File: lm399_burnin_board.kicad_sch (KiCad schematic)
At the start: 12 parts, among them J1 C64AC, J2 DB50_Female, U26 LT1085-ADJ

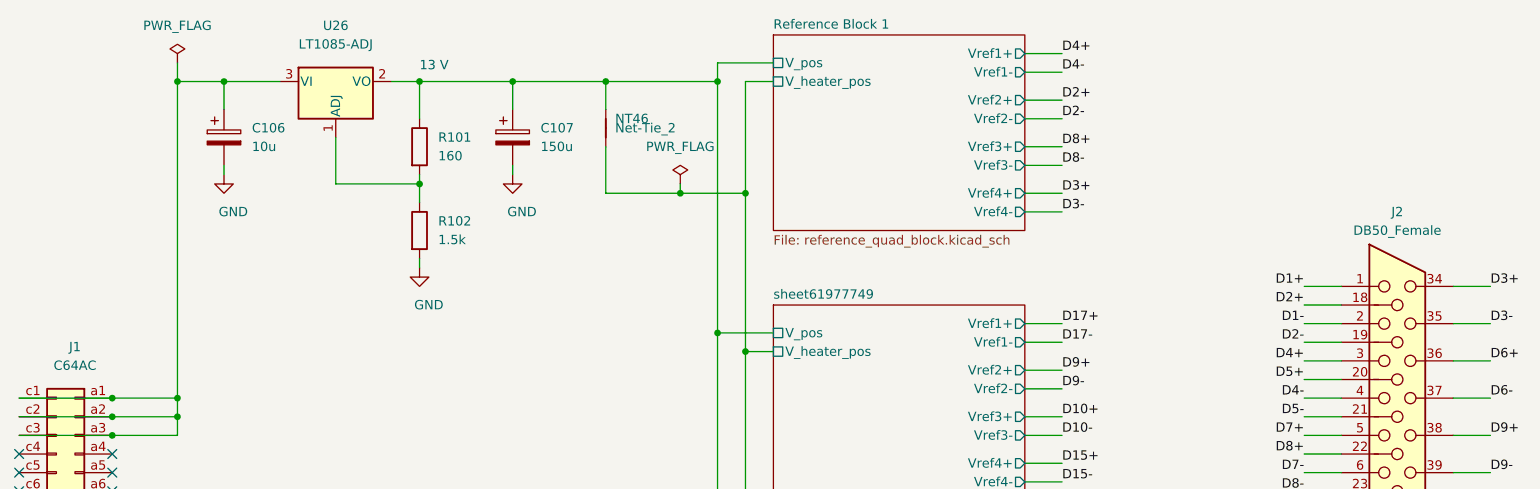
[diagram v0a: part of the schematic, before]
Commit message: Updated references to follow geographical rules
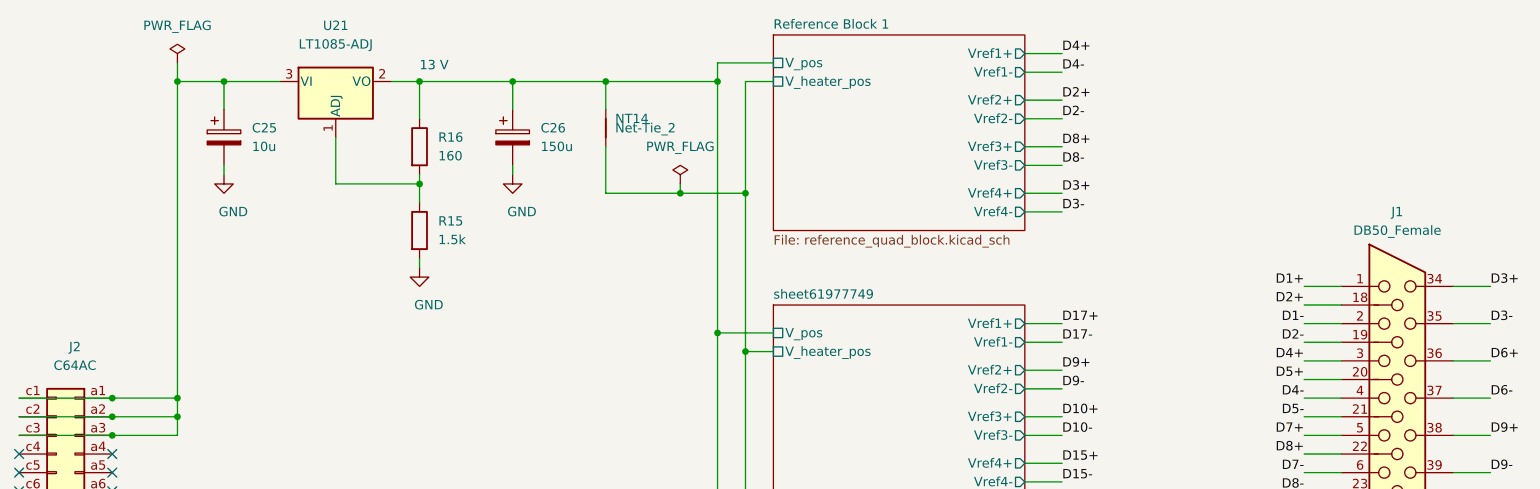
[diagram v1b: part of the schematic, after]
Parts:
- renumbered C106 to C25, C107 to C26, J2 to J1, J1 to J2, NT46 to NT14, R102 to R15, R101 to R16, U26 to U21
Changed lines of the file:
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@@
 		(on_board yes)
 		(dnp no)
-		(property "Reference" "J1"
+		(property "Reference" "J2"
 			(at 26.67 60.325 0)
 			(effects
@@
 			(project "lm399_burnin_board"
 				(path "/6284122b-79c3-4e04-925e-3d32cc3ec077"
-					(reference "J1")
+					(reference "J2")
 					(unit 1)
 				)
@@
 		(on_board yes)
 		(dnp no)
-		(property "Reference" "J2"
+		(property "Reference" "J1"
 			(at 207.01 41.91 0)
 			(effects
@@
 			(project "main"
 				(path "/6284122b-79c3-4e04-925e-3d32cc3ec077"
-					(reference "J2")
+					(reference "J1")
 					(unit 1)
 				)
@@
 		(on_board yes)
 		(dnp no)
-		(property "Reference" "U26"
+		(property "Reference" "U21"
 			(at 62.23 16.51 0)
 			(effects
@@
 			(project "main"
 				(path "/6284122b-79c3-4e04-925e-3d32cc3ec077"
-					(reference "U26")
+					(reference "U21")
 					(unit 1)
 				)
@@
 		(on_board yes)
 		(dnp no)
-		(property "Reference" "C106"
+		(property "Reference" "C25"
 			(at 50.8 30.48 0)
 			(effects
@@
 			(project "main"
 				(path "/6284122b-79c3-4e04-925e-3d32cc3ec077"
-					(reference "C106")
+					(reference "C25")
 					(unit 1)
 				)
@@
 		(on_board yes)
 		(dnp no)
-		(property "Reference" "C107"
+		(property "Reference" "C26"
 			(at 90.17 30.48 0)
 			(effects
@@
 			(project "main"
 				(path "/6284122b-79c3-4e04-925e-3d32cc3ec077"
-					(reference "C107")
+					(reference "C26")
 					(unit 1)
 				)
@@
 		(on_board yes)
 		(dnp no)
-		(property "Reference" "R101"
+		(property "Reference" "R16"
 			(at 76.2 31.75 0)
 			(effects
@@
 			(project "main"
 				(path "/6284122b-79c3-4e04-925e-3d32cc3ec077"
-					(reference "R101")
+					(reference "R16")
 					(unit 1)
 				)
@@
 		(on_board yes)
 		(dnp no)
-		(property "Reference" "R102"
+		(property "Reference" "R15"
 			(at 76.2 43.18 0)
 			(effects
@@
 			(project "main"
 				(path "/6284122b-79c3-4e04-925e-3d32cc3ec077"
-					(reference "R102")
+					(reference "R15")
 					(unit 1)
 				)
@@
 		(on_board yes)
 		(dnp no)
-		(property "Reference" "NT46"
+		(property "Reference" "NT14"
 			(at 100.33 29.21 90)
 			(effects
@@
 			(project "main"
 				(path "/6284122b-79c3-4e04-925e-3d32cc3ec077"
-					(reference "NT46")
+					(reference "NT14")
 					(unit 1)
 				)

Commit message: Fixed footprints
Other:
- sheet sheet61977749 renamed Reference Block 2
- sheet sheet61977B89 renamed Reference Block 3
- sheet sheet6197811F renamed Reference Block 4
- sheet sheet6197BEAD renamed Reference Block 5
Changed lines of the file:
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@@
 			)
 		)
-		(property "Datasheet" " ~"
+		(property "Datasheet" "~"
 			(at 182.88 80.01 0)
 			(effects
@@
 		(at 256.54 171.45 0)
 		(unit 1)
-		(exclude_from_sim no)
+		(exclude_from_sim yes)
 		(in_bom yes)
 		(on_board yes)
@@
 		)
 		(property "PN" ""
-			(at 256.54 171.45 0)
-			(effects
-				(font
-					(size 1.27 1.27)
-				)
-				(hide yes)
-			)
-		)
-		(property "Sim.Enable" "0"
 			(at 256.54 171.45 0)
 			(effects
@@
 			(color 0 0 0 0.0000)
 		)
-		(property "Sheetname" "sheet61977749"
+		(property "Sheetname" "Reference Block 2"
 			(at 121.92 53.8984 0)
 			(effects
@@
 			(color 0 0 0 0.0000)
 		)
-		(property "Sheetname" "sheet61977B89"
+		(property "Sheetname" "Reference Block 3"
 			(at 121.92 90.7284 0)
 			(effects
@@
 			(color 0 0 0 0.0000)
 		)
-		(property "Sheetname" "sheet6197811F"
+		(property "Sheetname" "Reference Block 4"
 			(at 121.92 127.5584 0)
 			(effects
@@
 			(color 0 0 0 0.0000)
 		)
-		(property "Sheetname" "sheet6197BEAD"
+		(property "Sheetname" "Reference Block 5"
 			(at 121.92 164.3884 0)
 			(effects

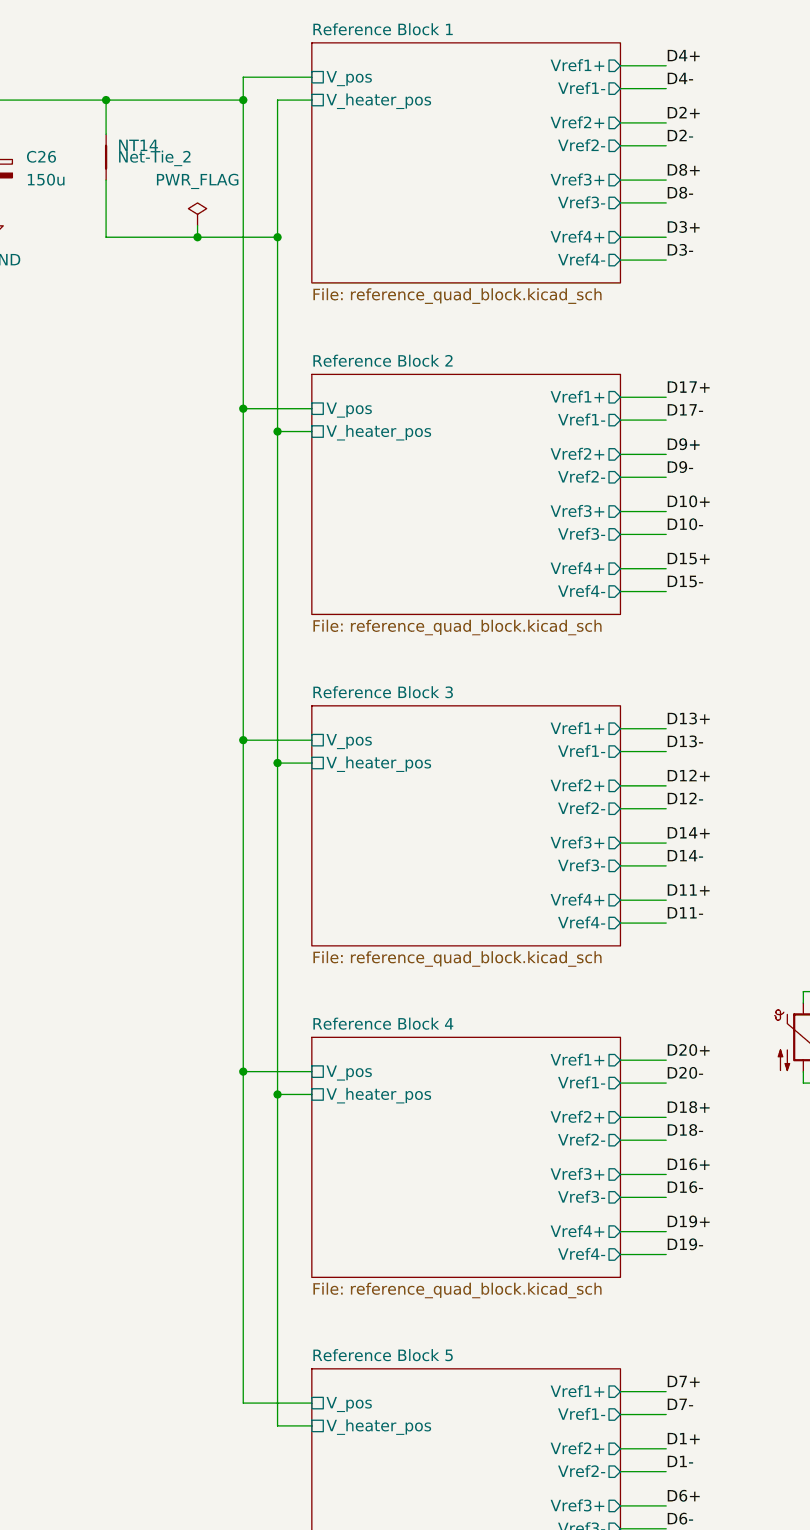
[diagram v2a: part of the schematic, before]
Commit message: Added CI (#6)
* Added CI

* Added RoHS info

* Fixed silkscreen labels
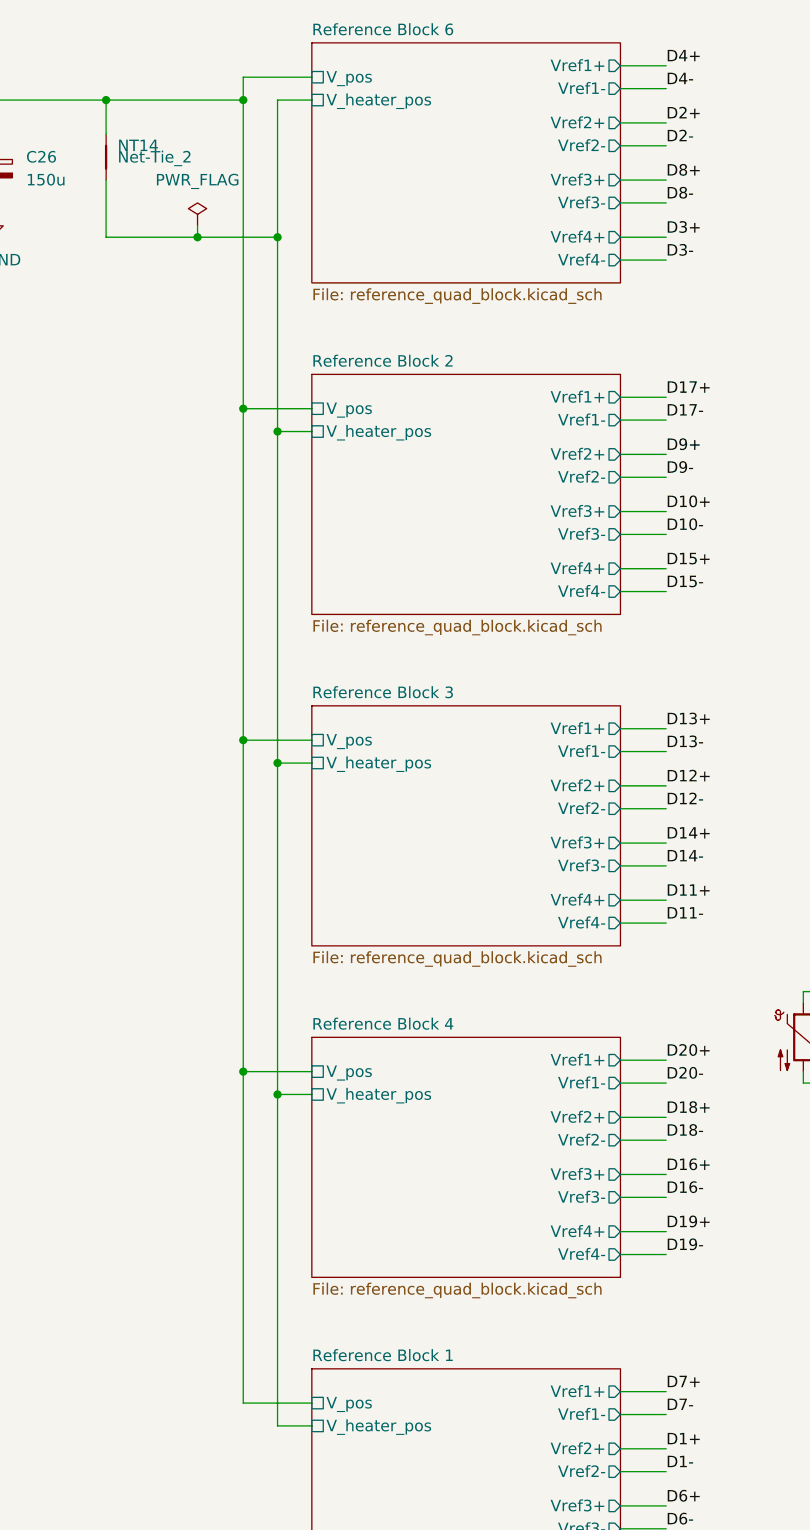
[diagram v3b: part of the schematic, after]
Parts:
- C25, C26: RoHS (none) -> Yes; Temperature (none) -> Tstorage = –55 °C to 105 °C
- J1: RoHS (none) -> Yes; Temperature (none) -> Tstorage = –55 °C to 125 °C
- J2: MFN Erni -> HARTING; PN 364914 -> 09031646921; RoHS (none) -> Yes; Temperature (none) -> Tstorage = –55 °C to 125 °C
- R15, R16: RoHS (none) -> By exemption; Temperature (none) -> Tstorage = –55 °C to 155 °C
- TH1, TH2: RoHS (none) -> Yes; Temperature (none) -> Tstorage = –40 °C to 150 °C
- U21: RoHS (none) -> By exemption; Temperature (none) -> Tstorage = –40 °C to 150 °C
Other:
- removed sheet Reference Block 5
- added sheet Reference Block 6 (reference_quad_block.kicad_sch)
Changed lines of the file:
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@@
 			)
 		)
-		(property "Description" ""
+		(property "Description" "DIN41612 connector, double row (AC), 02x32, script generated (kicad-library-utils/schlib/autogen/connector/)"
 			(at 26.67 105.41 0)
 			(effects
@@
 			)
 		)
-		(property "MFN" "Erni"
+		(property "MFN" "HARTING"
 			(at 26.67 105.41 0)
 			(effects
@@
 			)
 		)
-		(property "PN" "364914"
+		(property "PN" "09031646921"
 			(at 26.67 105.41 0)
 			(effects
@@
 		)
 		(property "Alternative" "ept 103-40035"
+			(at 26.67 105.41 0)
+			(effects
+				(font
+					(size 1.27 1.27)
+				)
+				(hide yes)
+			)
+		)
+		(property "RoHS" "Yes"
+			(at 26.67 105.41 0)
+			(effects
+				(font
+					(size 1.27 1.27)
+				)
+				(hide yes)
+			)
+		)
+		(property "Temperature" "Tstorage = –55 °C to 125 °C"
 			(at 26.67 105.41 0)
 			(effects
@@
 			)
 		)
+		(property "RoHS" "Yes"
+			(at 207.01 92.71 0)
+			(effects
+				(font
+					(size 1.27 1.27)
+				)
+				(hide yes)
+			)
+		)
+		(property "Temperature" "Tstorage = –55 °C to 125 °C"
+			(at 207.01 92.71 0)
+			(effects
+				(font
+					(size 1.27 1.27)
+				)
+				(hide yes)
+			)
+		)
 		(pin "0"
 		)
@@
 			)
 		)
+		(property "RoHS" "By exemption"
+			(at 62.23 24.13 0)
+			(effects
+				(font
+					(size 1.27 1.27)
+				)
+				(hide yes)
+			)
+		)
+		(property "Temperature" "Tstorage = –40 °C to 150 °C"
+			(at 62.23 24.13 0)
+			(effects
+				(font
+					(size 1.27 1.27)
+				)
+				(hide yes)
+			)
+		)
 		(pin "1"
 		)
@@
 			)
 		)
+		(property "RoHS" "Yes"
+			(at 46.99 31.75 0)
+			(effects
+				(font
+					(size 1.27 1.27)
+				)
+				(hide yes)
+			)
+		)
+		(property "Temperature" "Tstorage = –55 °C to 105 °C"
+			(at 46.99 31.75 0)
+			(effects
+				(font
+					(size 1.27 1.27)
+				)
+				(hide yes)
+			)
+		)
 		(pin "1"
 		)
@@
 			)
 		)
+		(property "RoHS" "Yes"
+			(at 86.36 31.75 0)
+			(effects
+				(font
+					(size 1.27 1.27)
+				)
+				(hide yes)
+			)
+		)
+		(property "Temperature" "Tstorage = –55 °C to 105 °C"
+			(at 86.36 31.75 0)
+			(effects
+				(font
+					(size 1.27 1.27)
+				)
+				(hide yes)
+			)
+		)
 		(pin "1"
 		)
@@
 			)
 		)
+		(property "RoHS" "By exemption"
+			(at 73.66 33.02 0)
+			(effects
+				(font
+					(size 1.27 1.27)
+				)
+				(hide yes)
+			)
+		)
+		(property "Temperature" "Tstorage = –55 °C to 155 °C"
+			(at 73.66 33.02 0)
+			(effects
+				(font
+					(size 1.27 1.27)
+				)
+				(hide yes)
+			)
+		)
 		(pin "1"
 		)
@@
 			)
 		)
+		(property "RoHS" "By exemption"
+			(at 73.66 44.45 0)
+			(effects
+				(font
+					(size 1.27 1.27)
+				)
+				(hide yes)
+			)
+		)
+		(property "Temperature" "Tstorage = –55 °C to 155 °C"
+			(at 73.66 44.45 0)
+			(effects
+				(font
+					(size 1.27 1.27)
+				)
+				(hide yes)
+			)
+		)
 		(pin "1"
 		)
@@
 			)
 		)
+		(property "Sim.Enable" "0"
+			(at 0 342.9 0)
+			(effects
+				(font
+					(size 1.27 1.27)
+				)
+				(hide yes)
+			)
+		)
 		(instances
 			(project "main"
@@
 			)
 		)
+		(property "RoHS" "Yes"
+			(at 176.53 128.27 0)
+			(effects
+				(font
+					(size 1.27 1.27)
+				)
+				(hide yes)
+			)
+		)
+		(property "Temperature" "Tstorage = –40 °C to 150 °C"
+			(at 176.53 128.27 0)
+			(effects
+				(font
+					(size 1.27 1.27)
+				)
+				(hide yes)
+			)
+		)
 		(pin "1"
 		)
@@
 		)
 		(property "PN" "NTCG163JX103DT1S"
+			(at 186.69 134.62 0)
+			(effects
+				(font
+					(size 1.27 1.27)
+				)
+				(hide yes)
+			)
+		)
+		(property "RoHS" "Yes"
+			(at 186.69 134.62 0)
+			(effects
+				(font
+					(size 1.27 1.27)
+				)
+				(hide yes)
+			)
+		)
+		(property "Temperature" "Tstorage = –40 °C to 150 °C"
 			(at 186.69 134.62 0)
 			(effects
@@
 			(color 0 0 0 0.0000)
 		)
-		(property "Sheetname" "Reference Block 1"
+		(property "Sheetname" "Reference Block 6"
 			(at 121.92 17.0684 0)
 			(effects
@@
 			(color 0 0 0 0.0000)
 		)
-		(property "Sheetname" "Reference Block 5"
+		(property "Sheetname" "Reference Block 1"
 			(at 121.92 164.3884 0)
 			(effects
